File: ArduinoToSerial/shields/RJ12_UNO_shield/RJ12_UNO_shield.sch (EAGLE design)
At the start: 17 parts, among them CON1 RJ12, CON2 RJ12, CON3 RJ12, CON4 RJ12

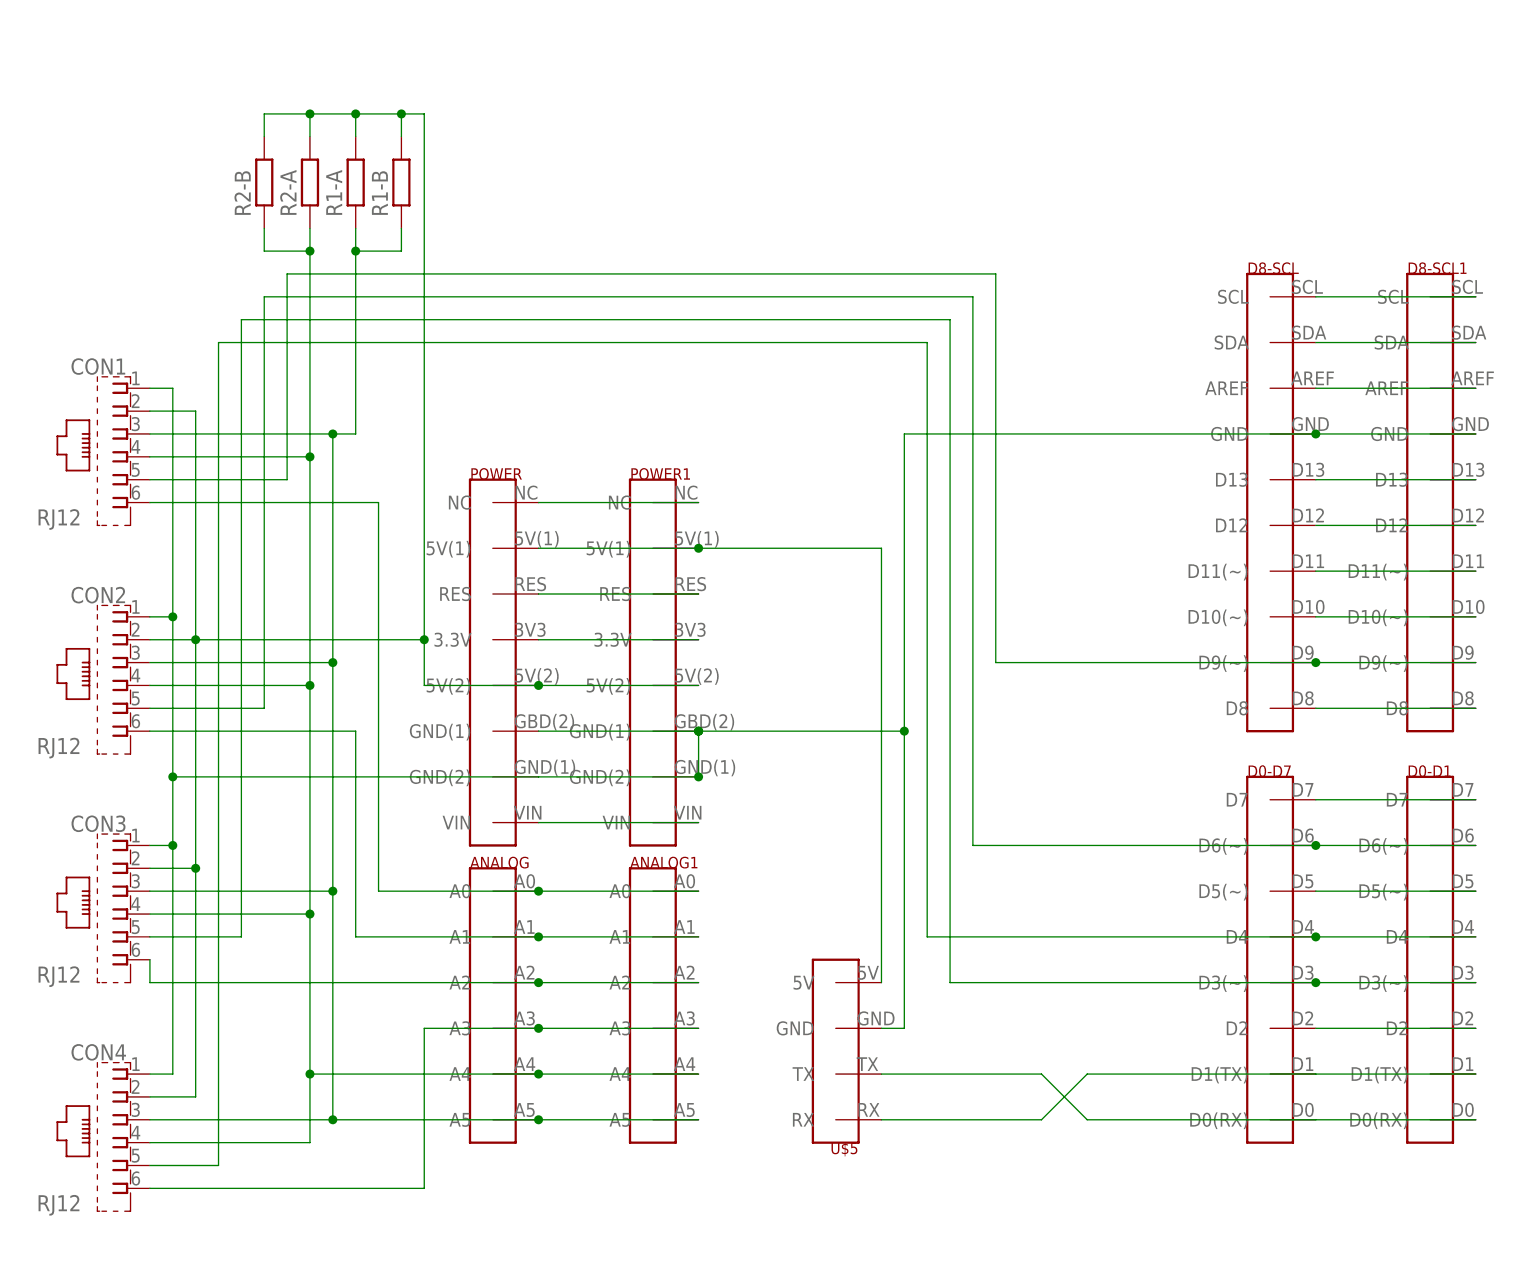
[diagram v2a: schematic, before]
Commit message: added THT + SMD resistor
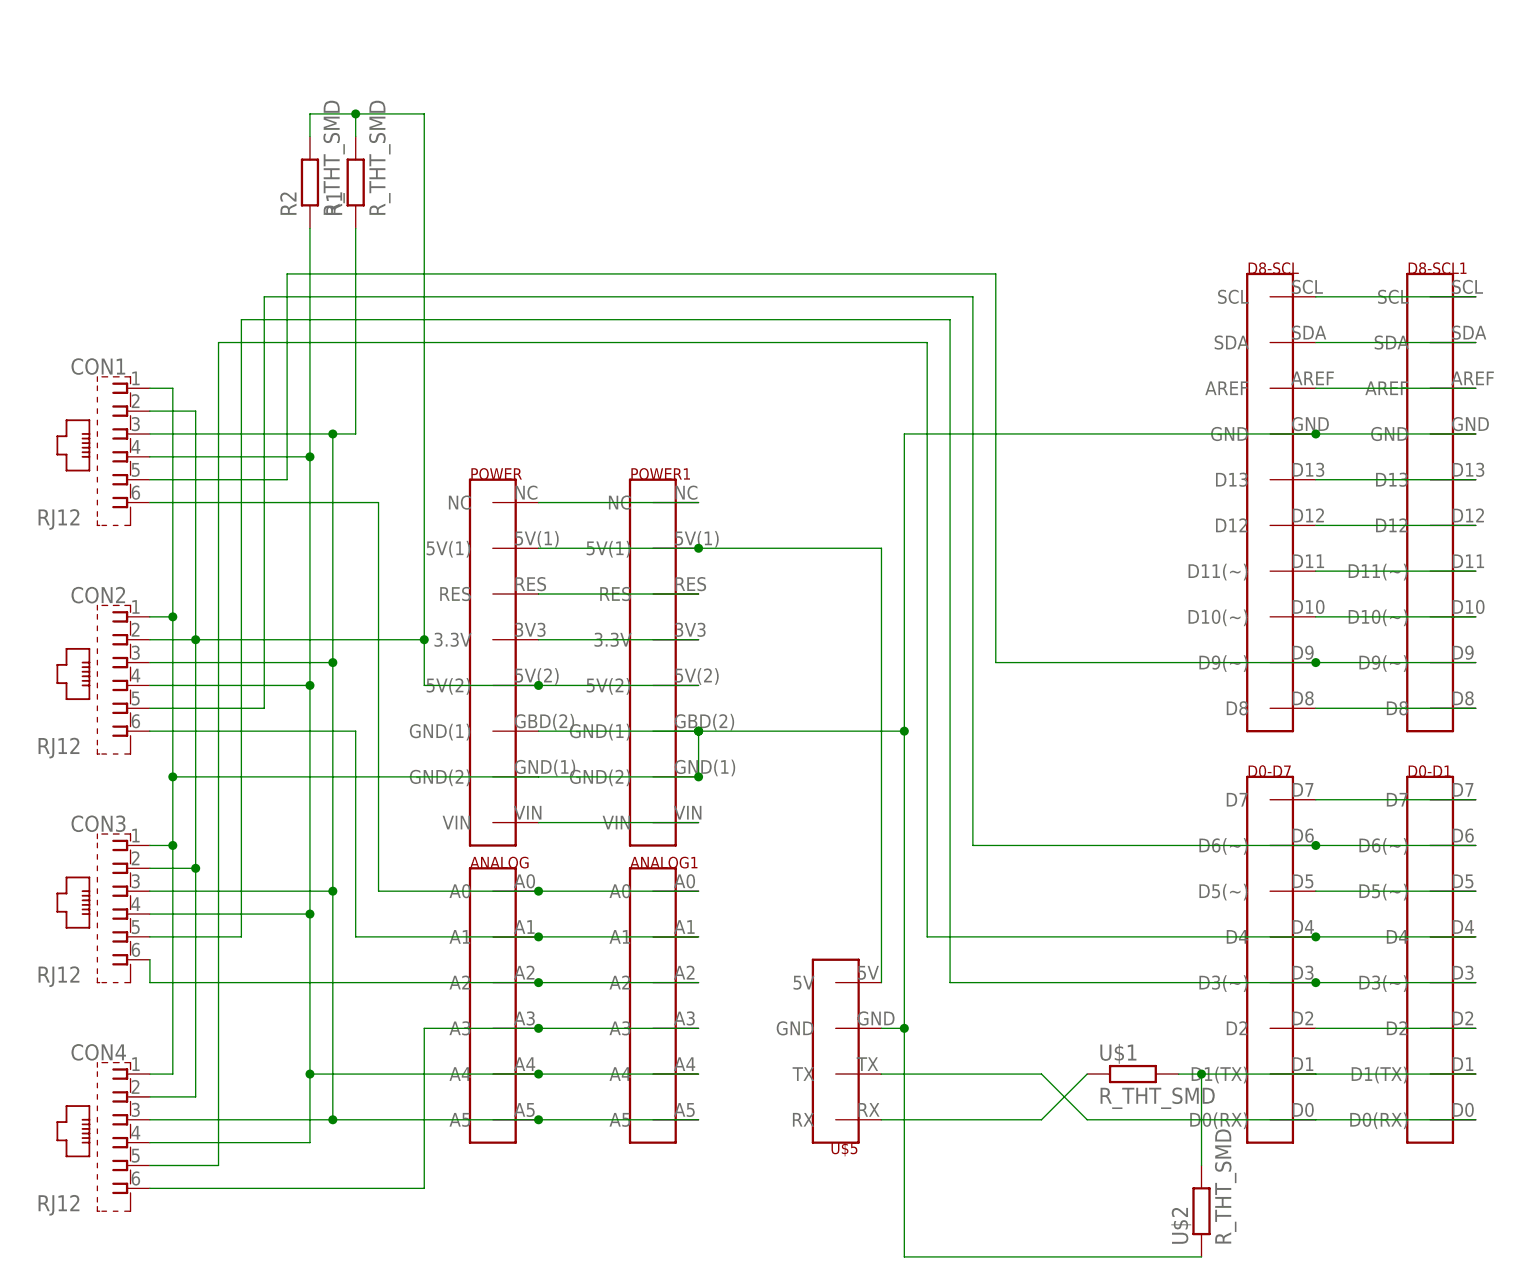
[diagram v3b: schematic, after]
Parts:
- removed R1-A, R2-A: (no value), resistor:R-EU_0207/10
- removed R1-B, R2-B: (no value), resistor:R-EU_R0805W
- added R1, R2, U$1, U$2: R_THT_SMD, AtoG:R_THT_SMD
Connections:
- new net N$21: D0-D1.D1(TX), D0-D7.D1(TX), U$1.2, U$2.2
- net GND: now also U$2.1
- net N$1: now also R1.1; no longer R1-A.1, R1-B.1
- net N$16: now also U$1.1; no longer D0-D1.D1(TX), D0-D7.D1(TX)
- net N$2: now also R2.1; no longer R2-A.1, R2-B.1
- net N$31: now also R1.2, R2.2; no longer R1-A.2, R1-B.2, R2-A.2, R2-B.2
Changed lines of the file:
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@@
 <part name="POWER1" library="AtoG" deviceset="POWER" device=""/>
 <part name="ANALOG1" library="AtoG" deviceset="ANALOG" device=""/>
-<part name="R1-A" library="resistor" deviceset="R-EU_" device="0207/10"/>
-<part name="R2-A" library="resistor" deviceset="R-EU_" device="0207/10"/>
-<part name="R2-B" library="resistor" deviceset="R-EU_" device="R0805W"/>
-<part name="R1-B" library="resistor" deviceset="R-EU_" device="R0805W"/>
+<part name="R1" library="AtoG" deviceset="R_THT_SMD" device=""/>
+<part name="R2" library="AtoG" deviceset="R_THT_SMD" device=""/>
+<part name="U$1" library="AtoG" deviceset="R_THT_SMD" device=""/>
+<part name="U$2" library="AtoG" deviceset="R_THT_SMD" device=""/>
 </parts>
 <sheets>
@@
 <instance part="POWER1" gate="G$1" x="33.02" y="50.8"/>
 <instance part="ANALOG1" gate="G$1" x="33.02" y="12.7"/>
-<instance part="R1-A" gate="G$1" x="0" y="104.14" rot="R90"/>
-<instance part="R2-A" gate="G$1" x="-5.08" y="104.14" rot="R90"/>
-<instance part="R2-B" gate="G$1" x="-10.16" y="104.14" rot="R90"/>
-<instance part="R1-B" gate="G$1" x="5.08" y="104.14" rot="R90"/>
+<instance part="R1" gate="G$1" x="0" y="104.14" rot="R90"/>
+<instance part="R2" gate="G$1" x="-5.08" y="104.14" rot="R90"/>
+<instance part="U$1" gate="G$1" x="86.36" y="5.08"/>
+<instance part="U$2" gate="G$1" x="93.98" y="-10.16" rot="R90"/>
 </instances>
 <busses>
@@
 <pinref part="CON1" gate="G$1" pin="3"/>
 <wire x1="-22.86" y1="76.2" x2="-2.54" y2="76.2" width="0.1524" layer="91"/>
-<pinref part="R1-A" gate="G$1" pin="1"/>
-<wire x1="0" y1="99.06" x2="0" y2="96.52" width="0.1524" layer="91"/>
+<pinref part="R1" gate="G$1" pin="1"/>
 <junction x="-2.54" y="76.2"/>
-<wire x1="0" y1="96.52" x2="0" y2="76.2" width="0.1524" layer="91"/>
+<wire x1="0" y1="99.06" x2="0" y2="76.2" width="0.1524" layer="91"/>
 <wire x1="0" y1="76.2" x2="-2.54" y2="76.2" width="0.1524" layer="91"/>
-<pinref part="R1-B" gate="G$1" pin="1"/>
-<wire x1="5.08" y1="99.06" x2="5.08" y2="96.52" width="0.1524" layer="91"/>
-<wire x1="5.08" y1="96.52" x2="0" y2="96.52" width="0.1524" layer="91"/>
-<junction x="0" y="96.52"/>
 </segment>
 </net>
@@
 <junction x="-5.08" y="22.86"/>
 <junction x="-5.08" y="48.26"/>
-<pinref part="R2-A" gate="G$1" pin="1"/>
-<wire x1="-5.08" y1="73.66" x2="-5.08" y2="96.52" width="0.1524" layer="91"/>
+<pinref part="R2" gate="G$1" pin="1"/>
+<wire x1="-5.08" y1="73.66" x2="-5.08" y2="99.06" width="0.1524" layer="91"/>
 <junction x="-5.08" y="73.66"/>
-<pinref part="R2-B" gate="G$1" pin="1"/>
-<wire x1="-5.08" y1="96.52" x2="-5.08" y2="99.06" width="0.1524" layer="91"/>
-<wire x1="-5.08" y1="96.52" x2="-10.16" y2="96.52" width="0.1524" layer="91"/>
-<wire x1="-10.16" y1="96.52" x2="-10.16" y2="99.06" width="0.1524" layer="91"/>
-<junction x="-5.08" y="96.52"/>
 </segment>
 </net>
@@
 <junction x="60.96" y="43.18"/>
 <junction x="106.68" y="76.2"/>
+<wire x1="60.96" y1="10.16" x2="60.96" y2="-15.24" width="0.1524" layer="91"/>
+<wire x1="60.96" y1="-15.24" x2="93.98" y2="-15.24" width="0.1524" layer="91"/>
+<junction x="60.96" y="10.16"/>
+<pinref part="U$2" gate="G$1" pin="1"/>
 </segment>
 </net>
@@
 <net name="N$16" class="0">
 <segment>
-<pinref part="D0-D7" gate="G$1" pin="D1(TX)"/>
-<pinref part="D0-D1" gate="G$1" pin="D1(TX)"/>
-<wire x1="106.68" y1="5.08" x2="124.46" y2="5.08" width="0.1524" layer="91"/>
-<wire x1="106.68" y1="5.08" x2="81.28" y2="5.08" width="0.1524" layer="91"/>
 <wire x1="81.28" y1="5.08" x2="76.2" y2="0" width="0.1524" layer="91"/>
 <pinref part="U$5" gate="G$1" pin="RX"/>
 <wire x1="76.2" y1="0" x2="58.42" y2="0" width="0.1524" layer="91"/>
+<pinref part="U$1" gate="G$1" pin="1"/>
 </segment>
 </net>
@@
 <wire x1="7.62" y1="53.34" x2="-17.78" y2="53.34" width="0.1524" layer="91"/>
 <wire x1="7.62" y1="53.34" x2="7.62" y2="111.76" width="0.1524" layer="91"/>
-<pinref part="R2-A" gate="G$1" pin="2"/>
+<pinref part="R2" gate="G$1" pin="2"/>
 <wire x1="-5.08" y1="109.22" x2="-5.08" y2="111.76" width="0.1524" layer="91"/>
-<pinref part="R1-A" gate="G$1" pin="2"/>
+<pinref part="R1" gate="G$1" pin="2"/>
 <wire x1="-5.08" y1="111.76" x2="0" y2="111.76" width="0.1524" layer="91"/>
 <wire x1="0" y1="111.76" x2="0" y2="109.22" width="0.1524" layer="91"/>
-<wire x1="7.62" y1="111.76" x2="5.08" y2="111.76" width="0.1524" layer="91"/>
 <junction x="0" y="111.76"/>
 <junction x="7.62" y="53.34"/>
-<pinref part="R1-B" gate="G$1" pin="2"/>
-<wire x1="5.08" y1="111.76" x2="0" y2="111.76" width="0.1524" layer="91"/>
-<wire x1="5.08" y1="109.22" x2="5.08" y2="111.76" width="0.1524" layer="91"/>
-<pinref part="R2-B" gate="G$1" pin="2"/>
-<wire x1="-5.08" y1="111.76" x2="-10.16" y2="111.76" width="0.1524" layer="91"/>
-<wire x1="-10.16" y1="111.76" x2="-10.16" y2="109.22" width="0.1524" layer="91"/>
-<junction x="5.08" y="111.76"/>
-<junction x="-5.08" y="111.76"/>
+<wire x1="7.62" y1="111.76" x2="0" y2="111.76" width="0.1524" layer="91"/>
 </segment>
 </net>
@@
 </segment>
 </net>
+<net name="N$21" class="0">
+<segment>
+<pinref part="D0-D1" gate="G$1" pin="D1(TX)"/>
+<pinref part="D0-D7" gate="G$1" pin="D1(TX)"/>
+<wire x1="106.68" y1="5.08" x2="124.46" y2="5.08" width="0.1524" layer="91"/>
+<wire x1="91.44" y1="5.08" x2="93.98" y2="5.08" width="0.1524" layer="91"/>
+<wire x1="93.98" y1="5.08" x2="106.68" y2="5.08" width="0.1524" layer="91"/>
+<wire x1="93.98" y1="-5.08" x2="93.98" y2="5.08" width="0.1524" layer="91"/>
+<junction x="93.98" y="5.08"/>
+<pinref part="U$1" gate="G$1" pin="2"/>
+<pinref part="U$2" gate="G$1" pin="2"/>
+</segment>
+</net>
